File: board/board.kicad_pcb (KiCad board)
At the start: 2 copper layers, 93 x 29 mm, 5 parts, among them J1 022_battery_cells, J2 022_battery_cells, U1 BK-6223-TR, U2 BK-6223-TR

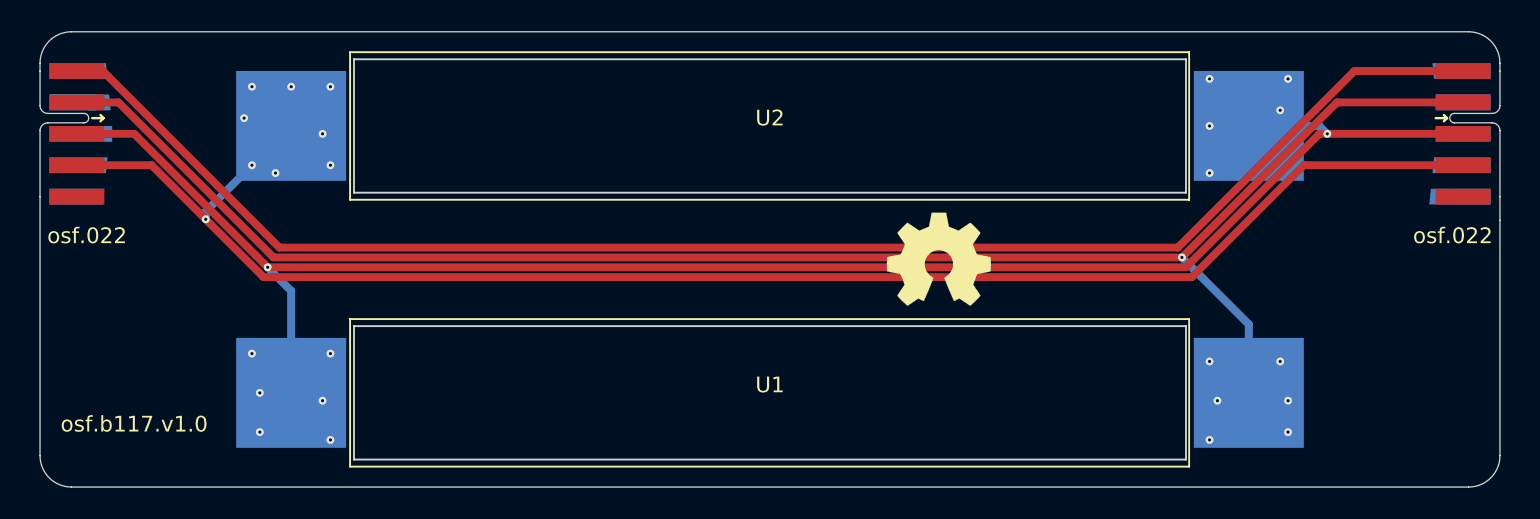
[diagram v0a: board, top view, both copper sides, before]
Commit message: improved hole geometry
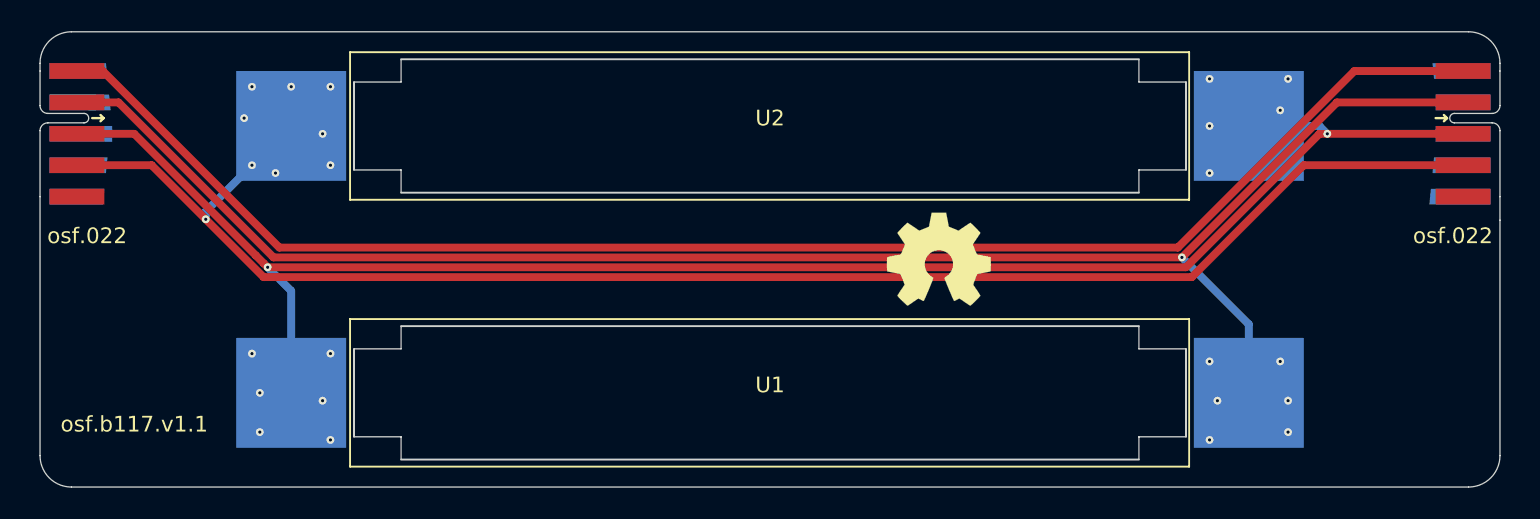
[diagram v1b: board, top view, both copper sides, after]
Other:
- board text added: "osf.b117.v1.1"
- board text removed: "osf.b117.v1.0"
